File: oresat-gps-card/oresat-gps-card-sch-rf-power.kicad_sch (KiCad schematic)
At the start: 29 parts, among them U15 SKY65723-81, U16 BP2G+, U17 MAX8510EXK29+T, U18 MAX8510EXK29+T, U19 MAX8510EXK33+T

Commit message: Routine Push
First attempt to clean up schematic
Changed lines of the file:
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@@
 		)
 	)
-	(global_label "MAX-RF"
+	(hierarchical_label "RF-IN"
 		(shape input)
-		(at 157.48 104.14 0)
-		(fields_autoplaced yes)
+		(at 81.28 101.6 180)
+		(effects
+			(font
+				(size 1.27 1.27)
+			)
+			(justify right)
+		)
+	)
+	(hierarchical_label "GPS-EN"
+		(shape input)
+		(at 269.24 167.64 180)
+		(effects
+			(font
+				(size 1.27 1.27)
+			)
+			(justify right)
+		)
+	)
+	(hierarchical_label "STQ-RF"
+		(shape input)
+		(at 157.48 99.06 0)
 		(effects
 			(font
@@
 			(justify left)
 		)
-		(property "Intersheetrefs" "${INTERSHEET_REFS}"
-			(at 167.5736 104.0606 0)
-			(show_name no)
-			(do_not_autoplace no)
-			(effects
-				(font
-					(size 1.27 1.27)
-				)
-				(justify left)
-			)
-		)
 	)
-	(global_label "RF-IN"
+	(hierarchical_label "MAX-RF"
 		(shape input)
-		(at 81.28 101.6 180)
-		(fields_autoplaced yes)
-		(effects
-			(font
-				(size 1.27 1.27)
-			)
-			(justify right)
-		)
-		(property "Intersheetrefs" "${INTERSHEET_REFS}"
-			(at 73.0007 101.5206 0)
-			(show_name no)
-			(do_not_autoplace no)
-			(effects
-				(font
-					(size 1.27 1.27)
-				)
-				(justify right)
-			)
-		)
-	)
-	(global_label "STQ-RF"
-		(shape input)
-		(at 157.48 99.06 0)
-		(fields_autoplaced yes)
+		(at 157.48 104.14 0)
 		(effects
 			(font
@@
 			(justify left)
 		)
-		(property "Intersheetrefs" "${INTERSHEET_REFS}"
-			(at 167.3317 98.9806 0)
-			(show_name no)
-			(do_not_autoplace no)
-			(effects
-				(font
-					(size 1.27 1.27)
-				)
-				(justify left)
-			)
-		)
 	)
-	(global_label "GPS-EN"
-		(shape input)
-		(at 269.24 167.64 180)
-		(fields_autoplaced yes)
-		(effects
-			(font
-				(size 1.27 1.27)
-			)
-			(justify right)
-		)
-		(property "Intersheetrefs" "${INTERSHEET_REFS}"
-			(at 259.0255 167.5606 0)
-			(show_name no)
-			(do_not_autoplace no)
-			(effects
-				(font
-					(size 1.27 1.27)
-				)
-				(justify right)
-			)
-		)
-	)

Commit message: Routine Push
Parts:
- removed TP95, TP96, TP97: 0.03x0.04, oresat-misc:TestPoint_Pad_D1.0mm, symbol oresat-misc:Test-Point-1mm-round
- C31, C32: footprint Capacitor_SMD:C_0805_2012Metric -> Capacitor_SMD:C_0603_1608Metric
- C37: footprint Capacitor_SMD:C_0402_1005Metric -> Capacitor_SMD:C_0603_1608Metric
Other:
- note added: "All resistors are 0603 1% AEC-Q200 unless marked. All capacitors are 0603 AEC-Q200 Vw >= 16V X5R or better unless marked."

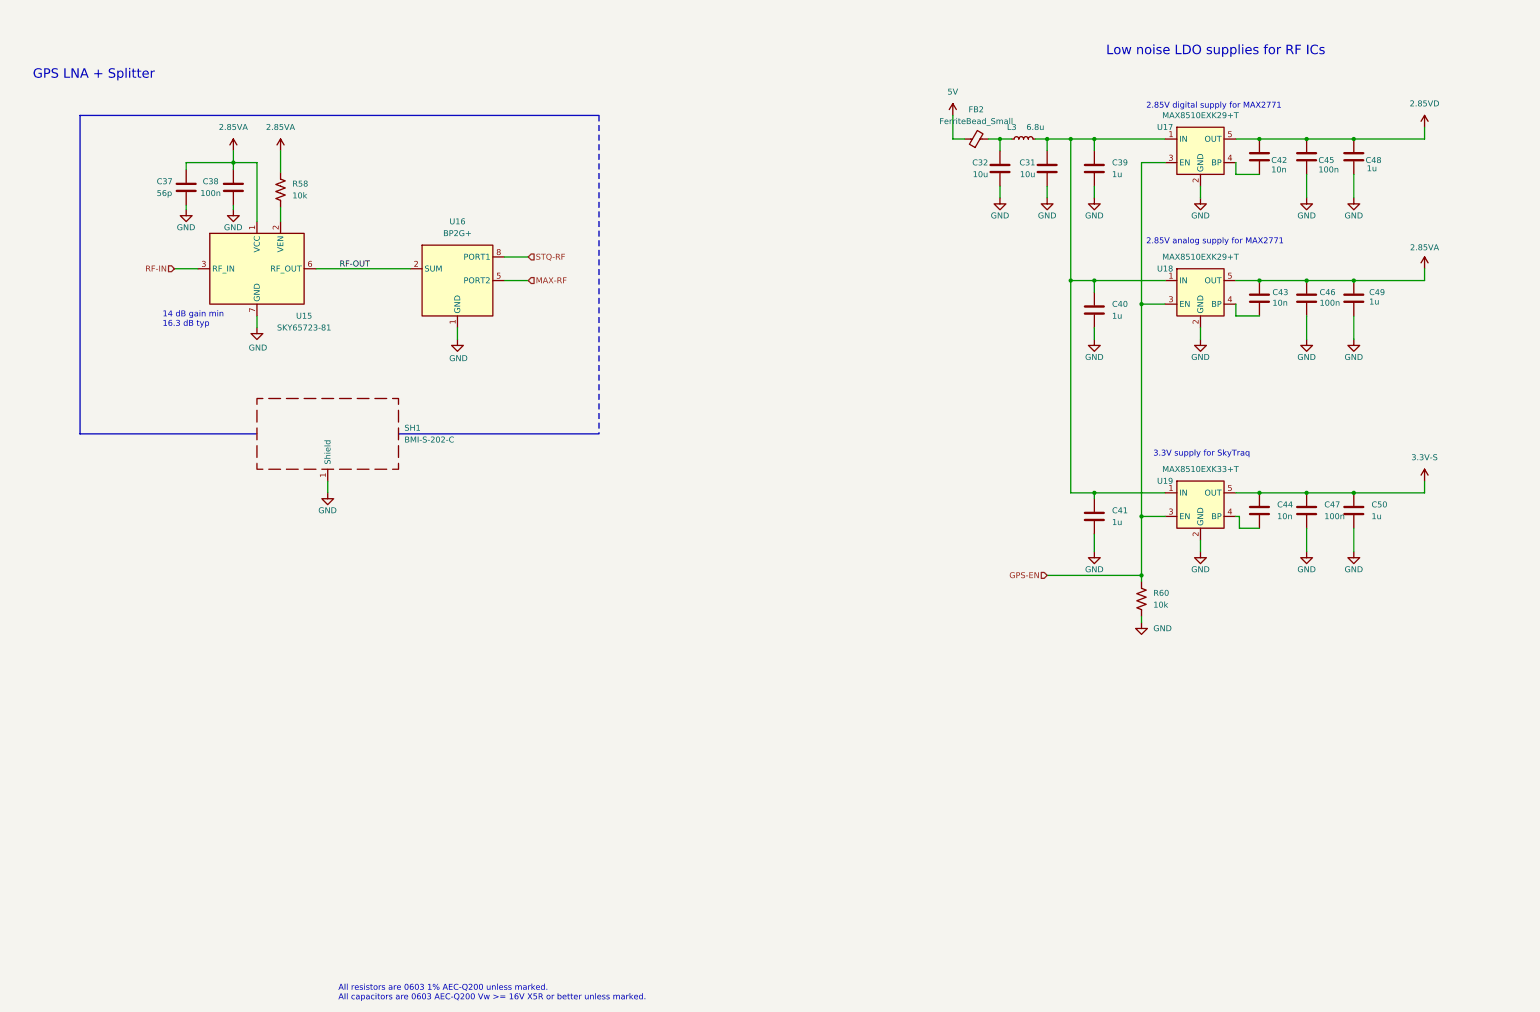
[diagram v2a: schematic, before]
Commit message: General cleanup of schematic and layout
Updated .gitignore, updates DRU file, moved RF lines to RF-50-MIN (max is just too big),
lots of cleanup on the root page to make it pretty, cleaned up some redudant labels,
updated SMPM connector and added rule zone, updated PCB outline to include NPTH drills
for SMPM connectors, began cleanup of OPD.
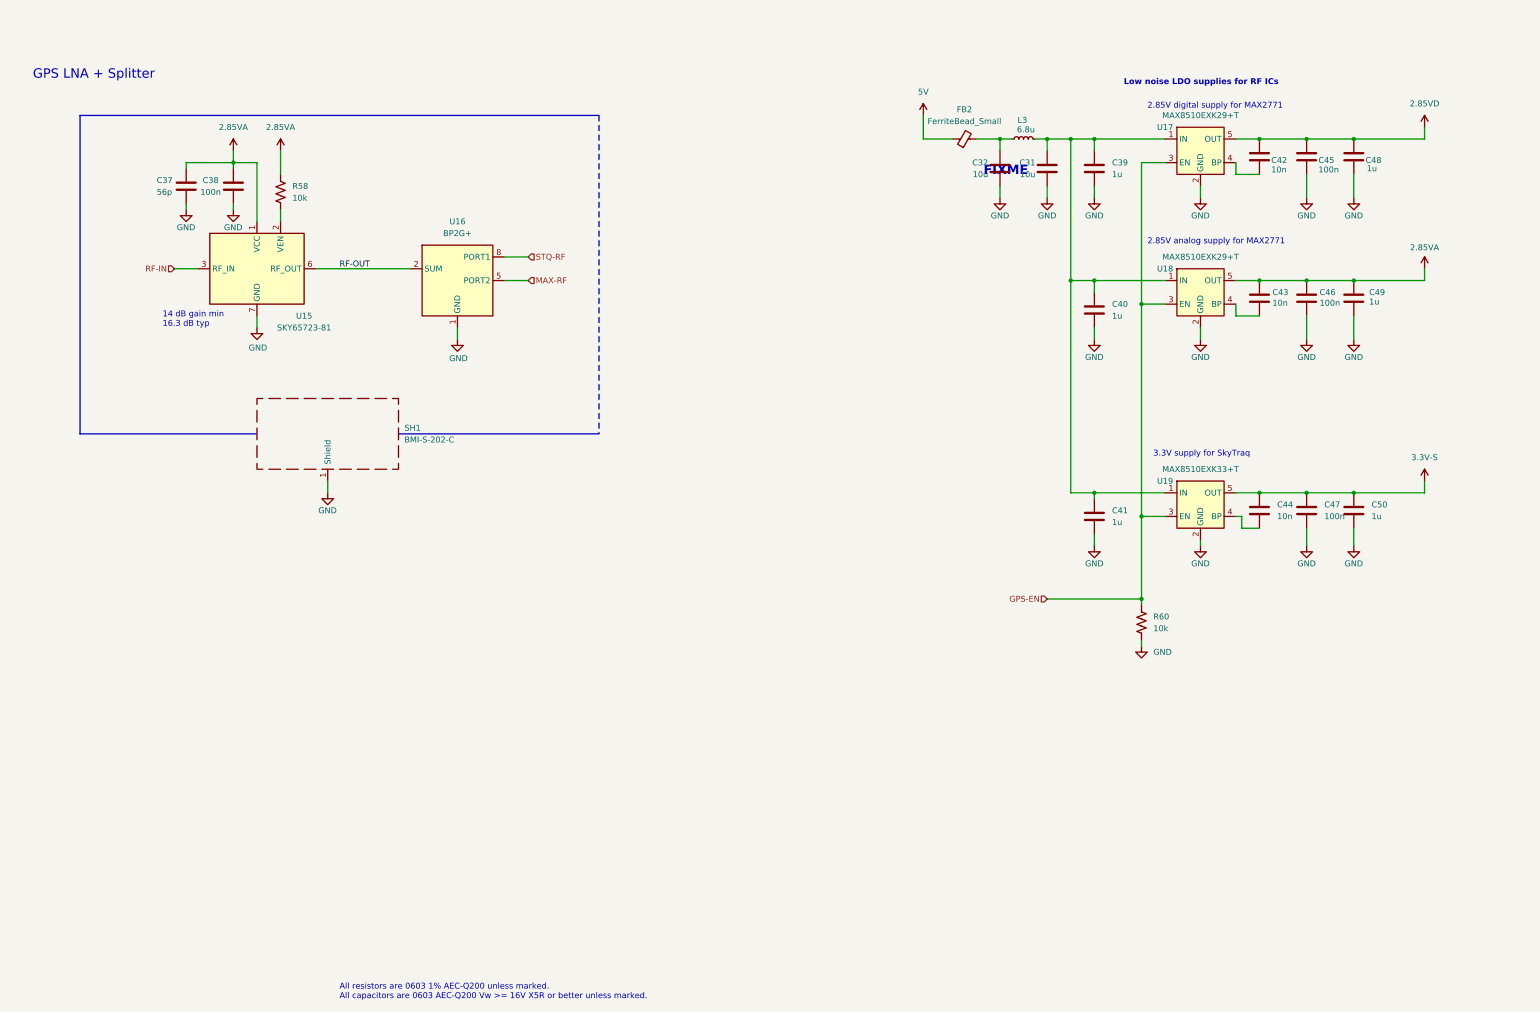
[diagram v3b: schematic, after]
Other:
- note added: "FIXME"
- moved on the sheet: FB2, R58, R60
